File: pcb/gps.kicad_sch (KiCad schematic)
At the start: 13 parts, among them J14 PPS, J15 U.FL, U12 MAX-M10S-00B

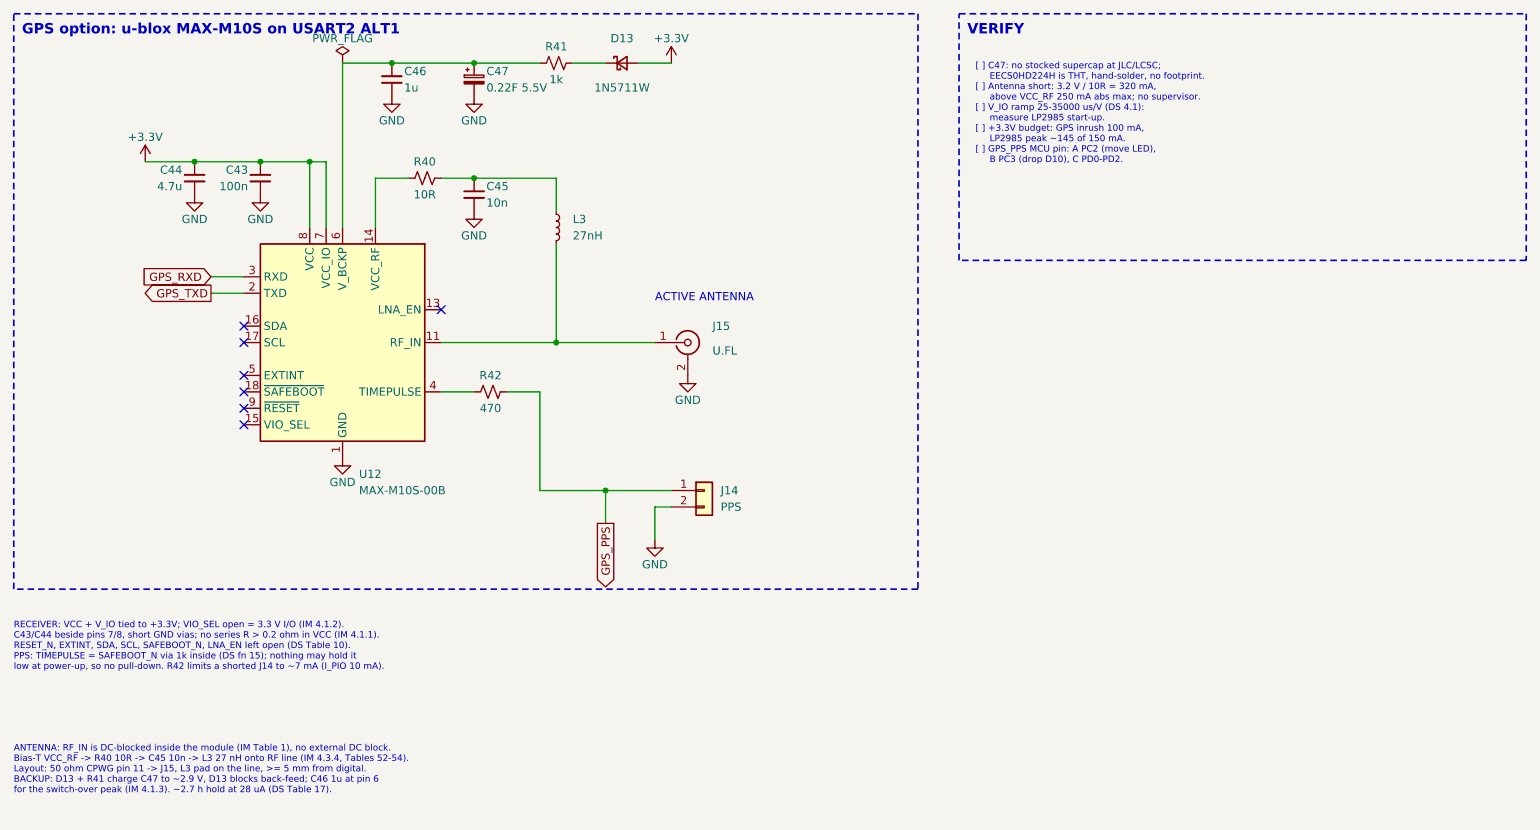
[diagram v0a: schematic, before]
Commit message: GPS fixes: TPS22941 antenna current limit, TLV75533 500 mA LDO, CR1220 V_BCKP
- U13 TPS22941 (C2653762) limits antenna short to 40-80 mA with auto-restart
  (avg <= 27 mA, was 320 mA); OC -> SDA as ANT_SHORT_N (IM 3.3.1.2)
- U11 LP2985 -> TLV75533PDBVR (C404027), C35 removed (pin 4 NC)
- C47/D13/R41 removed; BT1 CR1220 in KH-BS1220-2-SMT (C5365932)
- VERIFY updated
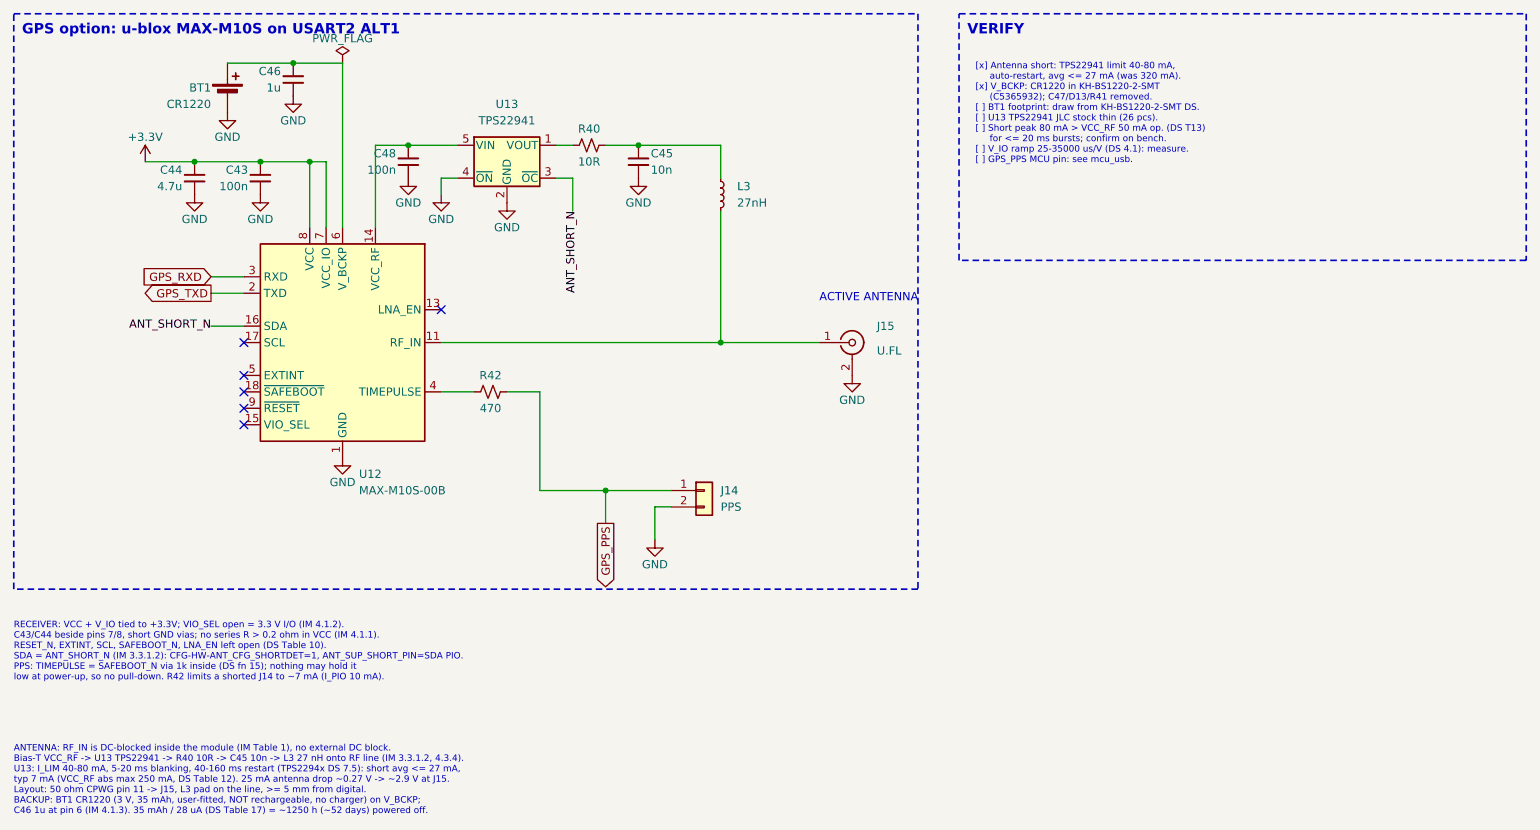
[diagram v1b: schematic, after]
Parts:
- removed C47: 0.22F 5.5V, symbol Device:C_Polarized_Small
- removed D13: 1N5711W, Diode_SMD:D_SOD-123, symbol Device:D_Schottky_Small
- removed R41: 1k, Resistor_SMD:R_0603_1608Metric, symbol Device:R_Small_US
- added BT1: CR1220, symbol Device:Battery_Cell
- added C48: 100n, Capacitor_SMD:C_0603_1608Metric, symbol Device:C_Small
- added U13: TPS22941, Package_TO_SOT_SMD:SOT-353_SC-70-5, symbol OpenBeacon2:TPS22941DCK
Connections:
- net GND: now also BT1.2 (-), C48.2, U13.2 (GND), U13.4 (~{ON})
- net at C46.1, U12.6 (V_BCKP): now also BT1.1 (+)
- net at R40.1: now also U13.1 (VOUT); no longer U12.14 (VCC_RF)
- net ANT_SHORT_N: now reaches U12.16 (SDA)
- net ANT_SHORT_N: now also U13.3 (~{OC})
- new net: C48.1, U12.14 (VCC_RF), U13.5 (VIN)
- no-connect marks 7 -> 6
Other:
- note added: "ANTENNA: RF_IN is DC-blocked inside the module (IM Table 1), no external DC block. Bias-T VCC_RF -> U13 TPS22941 -> R40 10R -> C45 10n -> L3 27 nH onto RF line (IM 3.3.1.2, 4.3.4). U13: I_LIM 40-80 mA, 5-20 ms blanking, 40-160 ms restart (TPS2294x DS 7.5): short avg <= 27 mA, typ 7 mA (VCC_RF abs max 250 mA, DS Table 12). 25 mA antenna drop ~0.27 V -> ~2.9 V at J15. Layout: 50 ohm CPWG pin 11 -> 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"
- note added: "RECEIVER: VCC + V_IO tied to +3.3V; VIO_SEL open = 3.3 V I/O (IM 4.1.2). C43/C44 beside pins 7/8, short GND vias; no series R > 0.2 ohm in VCC (IM 4.1.1). RESET_N, EXTINT, SCL, SAFEBOOT_N, LNA_EN left open (DS Table 10). SDA = ANT_SHORT_N (IM 3.3.1.2): CFG-HW-ANT_CFG_SHORTDET=1, ANT_SUP_SHORT_PIN=SDA PIO. PPS: TIMEPULSE = SAFEBOOT_N via 1k inside (DS fn 15); nothing may hold it low at power-up, s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"
- note added: "[x] Antenna short: TPS22941 limit 40-80 mA, auto-restart, avg <= 27 mA (was 320 mA). [x] V_BCKP: CR1220 in KH-BS1220-2-SMT (C5365932); C47/D13/R41 removed. [ ] BT1 footprint: draw from KH-BS1220-2-SMT DS. [ ] U13 TPS22941 JLC stock thin (26 pcs). [ ] Short peak 80 mA > VCC_RF 50 mA op. (DS T13) for <= 20 ms bursts; confirm on bench. [ ] V_IO ramp 25-35000 us/V (DS 4.1): measure. [ ] GPS_PPS MCU p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"
- note removed: "ANTENNA: RF_IN is DC-blocked inside the module (IM Table 1), no external DC block. Bias-T VCC_RF -> R40 10R -> C45 10n -> L3 27 nH onto RF line (IM 4.3.4, Tables 52-54). Layout: 50 ohm CPWG pin 11 -> J15, L3 pad on the line, >= 5 mm from digital. BACKUP: D13 + R41 charge C47 to ~2.9 V, D13 blocks back-feed; C46 1u at pin 6 for the switch-over peak (IM 4.1.3). ~2.7 h hold at 28 uA (DS Table 17)."
- note removed: "RECEIVER: VCC + V_IO tied to +3.3V; VIO_SEL open = 3.3 V I/O (IM 4.1.2). C43/C44 beside pins 7/8, short GND vias; no series R > 0.2 ohm in VCC (IM 4.1.1). RESET_N, EXTINT, SDA, SCL, SAFEBOOT_N, LNA_EN left open (DS Table 10). PPS: TIMEPULSE = SAFEBOOT_N via 1k inside (DS fn 15); nothing may hold it low at power-up, so no pull-down. R42 limits a shorted J14 to ~7 mA (I_PIO 10 mA)."
- note removed: "[ ] C47: no stocked supercap at JLC/LCSC; EECS0HD224H is THT, hand-solder, no footprint. [ ] Antenna short: 3.2 V / 10R = 320 mA, above VCC_RF 250 mA abs max; no supervisor. [ ] V_IO ramp 25-35000 us/V (DS 4.1): measure LP2985 start-up. [ ] +3.3V budget: GPS inrush 100 mA, LP2985 peak ~145 of 150 mA. [ ] GPS_PPS MCU pin: A PC2 (move LED), B PC3 (drop D10), C PD0-PD2."

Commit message: MCU: migrate to AVR128DA48-E/PT TQFP-48; GPS on USART3 PB0/PB1, GPS_PPS on async PF2 (EVSYS to TCB0 capture), per-pin decoupling
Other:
- note added: "GPS option: u-blox MAX-M10S on USART3 (PB0/PB1)"
- note removed: "GPS option: u-blox MAX-M10S on USART2 ALT1"
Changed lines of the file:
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@@
 		(rev "C")
 		(company "Etherkit")
-		(comment 1 "MAX-M10S on USART2 ALT1, PPS to J14, current-limited active-antenna bias-T, CR1220 V_BCKP")
+		(comment 1 "MAX-M10S on USART3 (PB0/PB1), PPS to J14, current-limited active-antenna bias-T, CR1220 V_BCKP")
 		(comment 4 "Creative Commons License CC-BY-SA")
 	)
@@
 		)
 	)
-	(text "GPS option: u-blox MAX-M10S on USART2 ALT1"
+	(text "GPS option: u-blox MAX-M10S on USART3 (PB0/PB1)"
 		(exclude_from_sim no)
 		(at 52.07 76.2 0)

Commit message: BT1: KH-BS1220-2-SMT footprint from LCSC C5365932; J6/J16: Si5351BCBreakout SMA-ENDLAUNCH footprint, BWSMA-KE-P001 C496550; project-local OB2 footprint lib
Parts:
- BT1: footprint (none) -> OB2:BAT-SMD_KH-CR1220-2
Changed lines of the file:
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@@
 			)
 		)
-		(property "Footprint" ""
+		(property "Footprint" "OB2:BAT-SMD_KH-CR1220-2"
 			(at 83.82 86.36 0)
 			(effects

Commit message: ESD: SP0503BAHT (C7074, already on BOM) at J4/J5 header pins + J14 PPS with 220R series (R64-R75, 0805 C17557 basic); ESD5V3U1U-02LRH (C3011174) on GPS RF_IN at U.FL J15; J5 moved under J4, header-side nets HDR_Dn; I2C level shift block moved right; regen PDF
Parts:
- added D17: SP0503BAHT, Package_TO_SOT_SMD:SOT-143, symbol Power_Protection:SP0503BAHT
- added D18: ESD5V3U1U-02LRH, Diode_SMD:D_SOD-882, symbol Device:D_Zener_Small
- added R75: 220R, Resistor_SMD:R_0805_2012Metric, symbol Device:R_Small_US
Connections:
- net GND: now also D17.1 (A), D18.2 (A)
- net GPS_PPS: now also R75.1; no longer J14.1 (Pin_1)
- net at J15.1 (In), L3.2, U12.11 (RF_IN): now also D18.1 (K)
- new net: D17.3 (K), J14.1 (Pin_1), R75.2
- no-connect marks 6 -> 8
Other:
- moved on the sheet: J14

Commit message: D18 on J15 GPS antenna: PESD5V0F1BL,315 (Nexperia, C45961) replaces TECH PUBLIC ESD5V3U1U copy (C3011174); Device:D_TVS_Small, SOD-882, same as D21; regen PDF
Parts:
- D18: value ESD5V3U1U-02LRH -> PESD5V0F1BL; symbol Device:D_Zener_Small -> Device:D_TVS_Small; LCSC C3011174 -> C45961; MPN ESD5V3U1U-02LRH -> PESD5V0F1BL,315; Manufacturer Infineon -> Nexperia
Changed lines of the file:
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@@
 	)
 	(symbol
-		(lib_id "Device:D_Zener_Small")
+		(lib_id "Device:D_TVS_Small")
 		(at 167.64 127 270)
 		(unit 1)
@@
 			)
 		)
-		(property "Value" "ESD5V3U1U-02LRH"
+		(property "Value" "PESD5V0F1BL"
 			(at 163.83 135.89 90)
 			(effects
@@
 			)
 		)
-		(property "Datasheet" ""
+		(property "Datasheet" "https://assets.nexperia.com/documents/data-sheet/PESD5V0F1BL.pdf"
 			(at 167.64 127 0)
 			(effects
@@
 			)
 		)
-		(property "MPN" "ESD5V3U1U-02LRH"
+		(property "MPN" "PESD5V0F1BL,315"
 			(at 167.64 127 0)
 			(effects
@@
 			)
 		)
-		(property "Manufacturer" "Infineon"
+		(property "Manufacturer" "Nexperia"
 			(at 167.64 127 0)
 			(effects
@@
 			)
 		)
-		(property "LCSC" "C3011174"
+		(property "LCSC" "C45961"
 			(at 167.64 127 0)
 			(effects
